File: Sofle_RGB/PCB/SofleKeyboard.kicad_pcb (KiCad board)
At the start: 2 copper layers, 143.4 x 111.8 mm, 97 parts, among them J1 LED, J2 4PIN, J3 OLED, J4 key leds, J5 backlight sel, J6 indicator bypass, P1 i2c_pin, P2 i2c_pin, SW1 SW_PUSH-MX_W_LED, SW10 SW_PUSH-MX_W_LED, SW11 SW_PUSH-MX_W_LED, SW12 SW_PUSH-MX_W_LED, SW13 SW_PUSH-MX_W_LED, SW14 SW_PUSH-MX_W_LED, SW15 SW_PUSH-MX_W_LED, SW16 SW_PUSH-MX_W_LED, SW17 SW_PUSH-MX_W_LED, SW18 SW_PUSH-MX_W_LED, SW19 SW_PUSH-MX_W_LED, SW2 SW_PUSH-MX_W_LED, SW20 SW_PUSH-MX_W_LED, SW21 SW_PUSH-MX_W_LED, SW22 SW_PUSH-MX_W_LED, SW23 SW_PUSH-MX_W_LED, SW24 SW_PUSH-MX_W_LED, SW25 Rotary_Encoder_Switch, SW26 SW_PUSH-MX_W_LED, SW27 SW_PUSH-MX_W_LED, SW28 SW_PUSH-MX_W_LED, SW29 SW_PUSH-MX_W_LED, SW3 SW_PUSH-MX_W_LED, SW30 SW_PUSH-MX_W_LED, SW4 SW_PUSH-MX_W_LED, SW5 SW_PUSH-MX_W_LED, SW6 SW_PUSH-MX_W_LED, SW7 SW_PUSH-MX_W_LED, SW8 SW_PUSH-MX_W_LED, SW9 SW_PUSH-MX_W_LED, U1 ProMicro

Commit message: updated gerbers, reviewed and happy for release
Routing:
- net GND: track 989.6 -> 987.1 mm, vias 124 -> 181
- net Net-(SW22-Pad3): track 56.5 -> 56.0 mm

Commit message: unknown changes
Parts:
- SW6: moved to F.Cu
- moved SW6 0.10 mm to (215.8, 52.4), turned to 180 degrees
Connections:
- SW6 pad 1: Net-(SW5-Pad3) -> (no net)
- SW6 pad 2: GND -> (no net)
- SW6 pad 3: Net-(SW12-Pad1) -> (no net)
- SW6 pad 4: VCC -> (no net)
- SW6 pad 5: Net-(D6-Pad2) -> (no net)
- SW6 pad 6: col0 -> (no net)
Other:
- board text added: "s1"
- board text added: "s10"
- board text added: "s11"
- board text added: "s12"
- board text added: "s13"
- board text added: "s14"
- board text added: "s15"
- board text added: "s16"
- board text added: "s17"
- board text added: "s18"
- board text added: "s19"
- board text added: "s2"
- board text added: "s20"
- board text added: "s21"
- board text added: "s22"
- board text added: "s23"
- board text added: "s24"
- board text added: "s26"
- board text added: "s27"
- board text added: "s28"
- board text added: "s29"
- board text added: "s3"
- board text added: "s30"
- board text added: "s4"
- board text added: "s5"
- board text added: "s6"
- board text added: "s7"
- board text added: "s8"
- board text added: "s9"

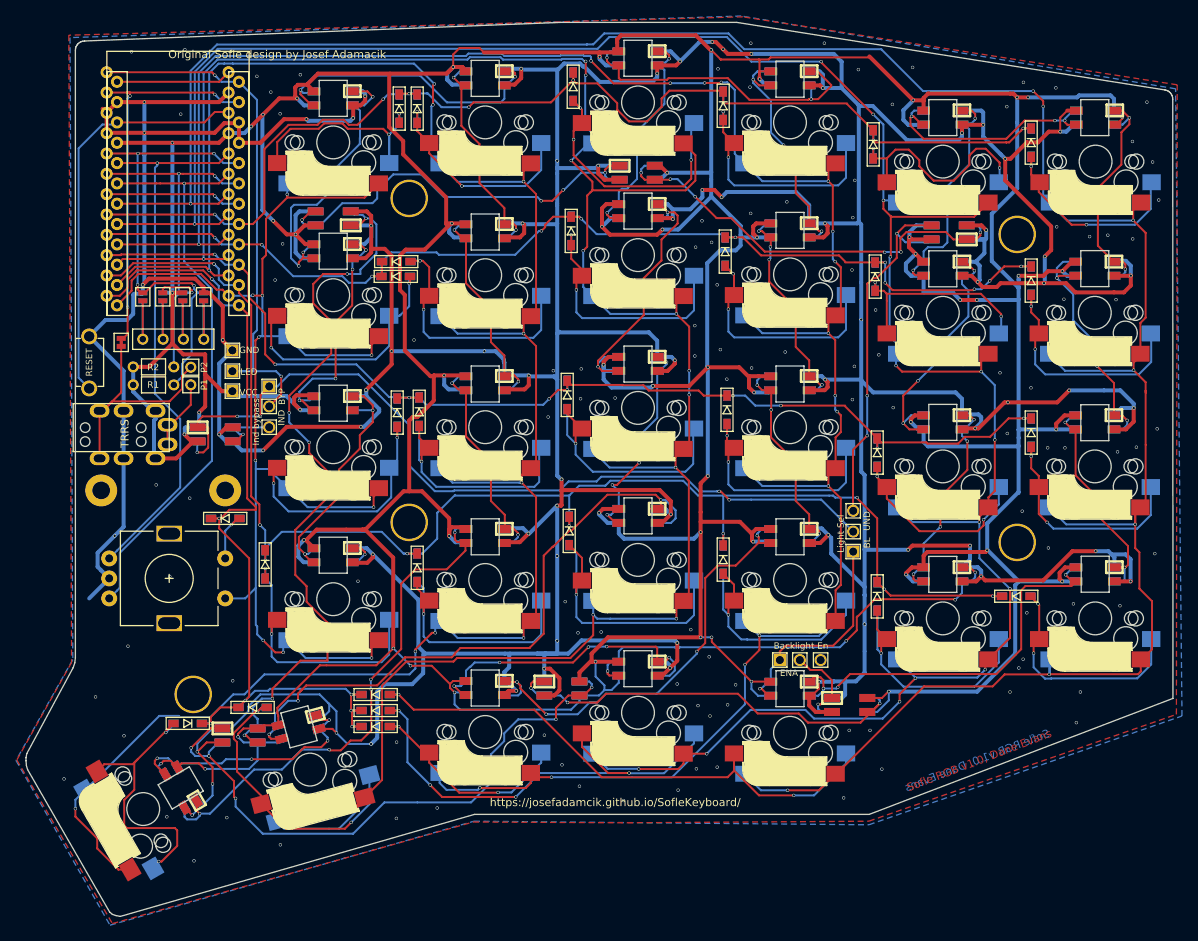
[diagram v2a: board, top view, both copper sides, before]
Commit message: updated pcb - flip key that was on bottom, fix led fix diode orientation fix some diode placement
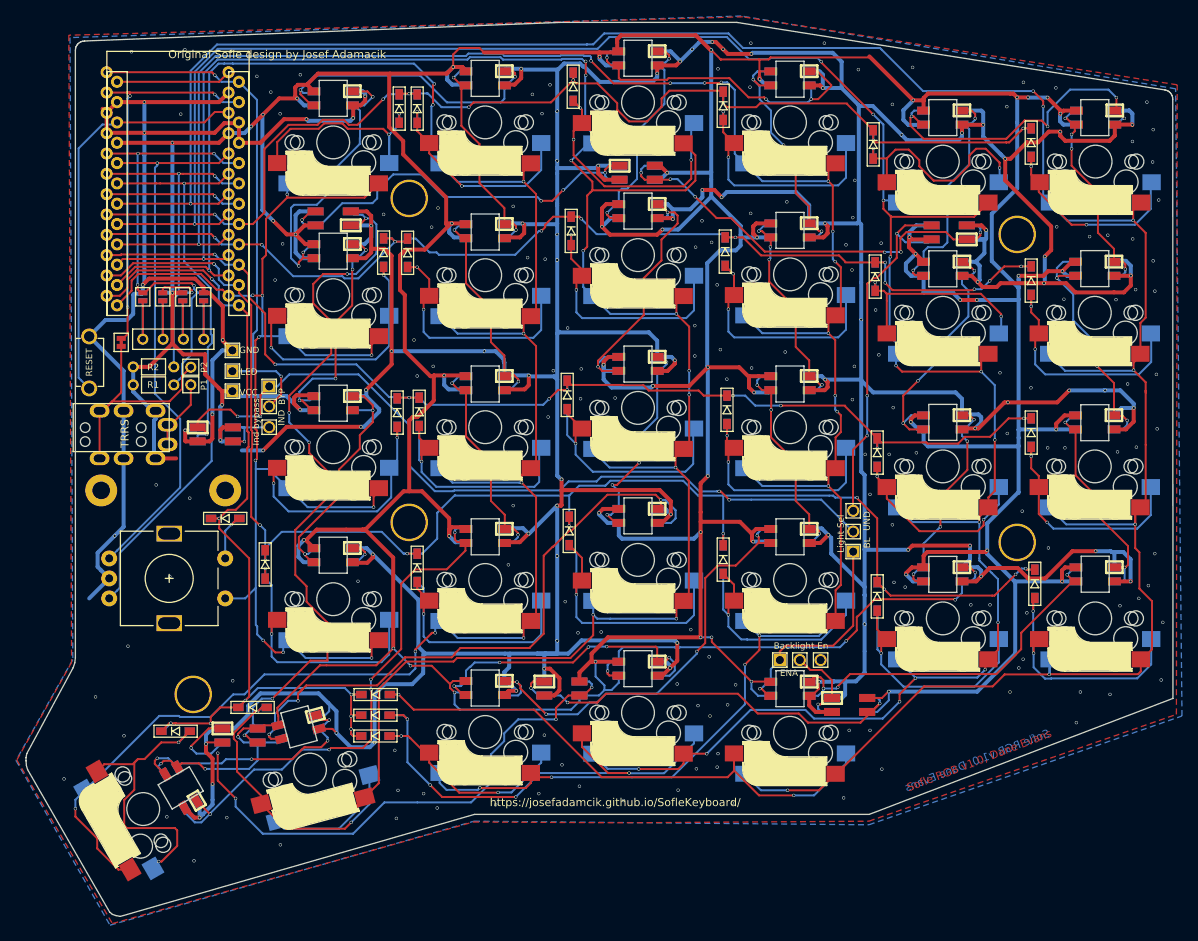
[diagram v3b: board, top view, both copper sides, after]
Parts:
- moved D7 3.34 mm to (126.8, 63.8), turned to 270 degrees
- moved D24 2.79 mm to (208.2, 105.2), turned to 270 degrees
- moved D26 1.81 mm to (100.8, 123.6), turned to 0 degrees
- moved D8 1.80 mm to (129.8, 63.8), turned to 270 degrees
- moved D28 1.18 mm to (125.8, 124.2)
- moved D29 0.58 mm to (125.8, 121.6)
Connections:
- D37 pad 2: VCC -> GND
- D37 pad 4: GND -> VCC
- SW6 pad 1: (no net) -> Net-(SW5-Pad3)
- SW6 pad 2: (no net) -> GND
- SW6 pad 3: (no net) -> Net-(SW12-Pad1)
- SW6 pad 4: (no net) -> VCC
- SW6 pad 5: (no net) -> Net-(D6-Pad2)
- SW6 pad 6: (no net) -> col0
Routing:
- net GND: track 987.1 -> 1001.1 mm, vias 181 -> 230
- net VCC: track 939.6 -> 928.4 mm, vias 56 -> 57
- net Net-(SW5-Pad3): track 31.2 -> 41.6 mm, vias 3 -> 4
- net row4: track 114.4 -> 120.5 mm, vias 7 -> 8
- net row3: track 183.2 -> 188.9 mm, vias 9 -> 10
- net Net-(SW24-Pad3): track 50.3 -> 46.8 mm
- net lights: track 106.2 -> 103.7 mm
- net Net-(D26-Pad2): track 35.7 -> 37.8 mm
- net row1: track 137.9 -> 139.9 mm
- net Net-(D24-Pad2): track 31.4 -> 33.3 mm
- net Net-(SW12-Pad1): track 30.3 -> 28.9 mm, vias 2 -> 4
- net col1: track 299.6 -> 298.5 mm
- net Net-(D29-Pad2): track 59.8 -> 60.9 mm
- net Net-(SW20-Pad3): track 66.2 -> 67.3 mm
- net Net-(D31-Pad1): track 95.2 -> 94.2 mm
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
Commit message: updated pcbs, starting documentation
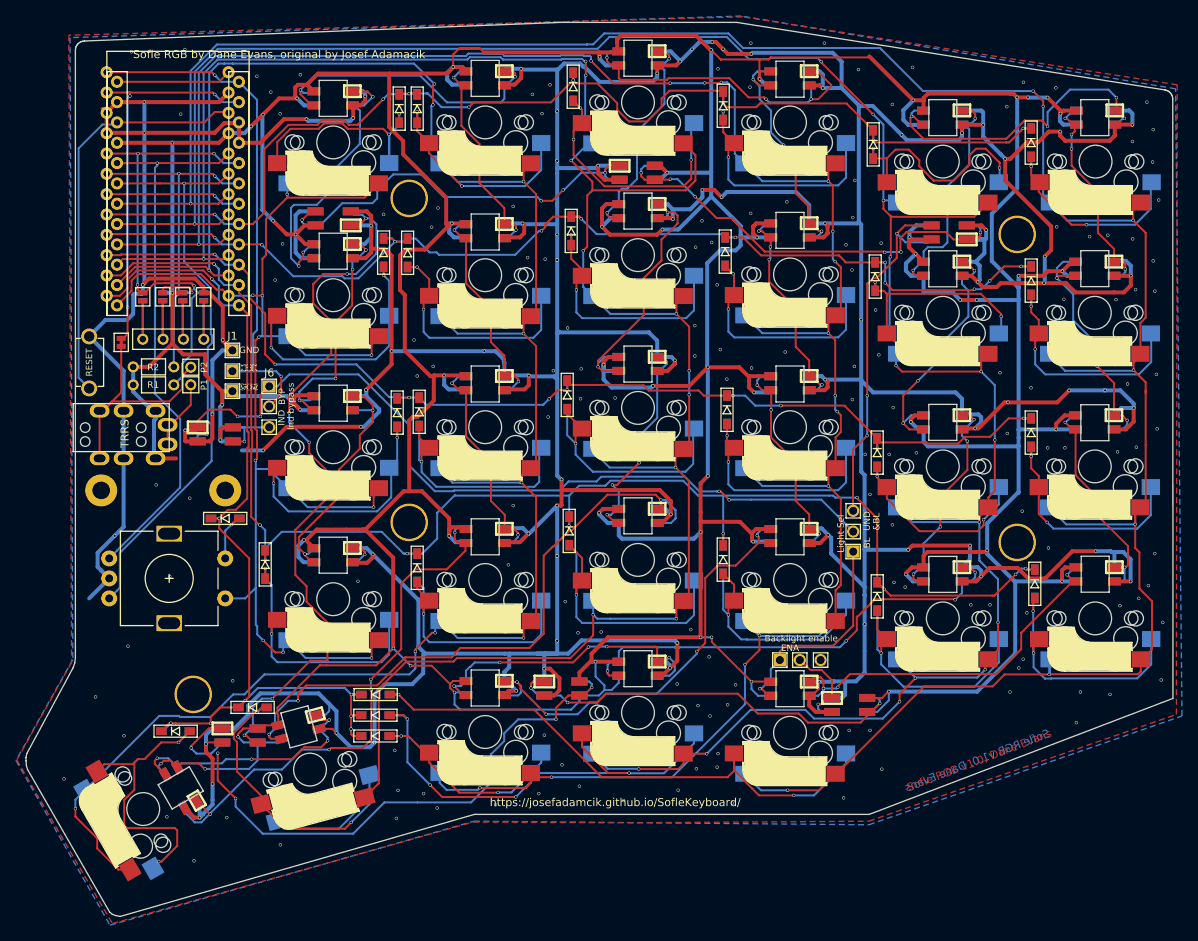
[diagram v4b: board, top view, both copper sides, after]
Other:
- board text added: "&BL"
- board text added: "Backlight enable"
- board text added: "Sofle RGB by Dane Evans, original by Josef Adamacik"
- board text removed: "Backlight En"
- board text removed: "Original Sofle design by Josef Adamacik"

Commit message: updated gerbers
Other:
- board text added: "Sofle RGB v2.0, Dane Evans"
- board text removed: "Sofle RGB v1.0, Dane Evans"
